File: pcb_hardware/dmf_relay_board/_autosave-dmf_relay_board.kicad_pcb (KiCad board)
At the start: 2 copper layers, 100 x 100 mm, 9 parts, among them J1 HVPS, J2 Relays to Electrodes 1, J3 Relays to Electrodes 2, J4 Electrodes from Relay 1, J5 Electrodes from Relay 2, U1 HV507

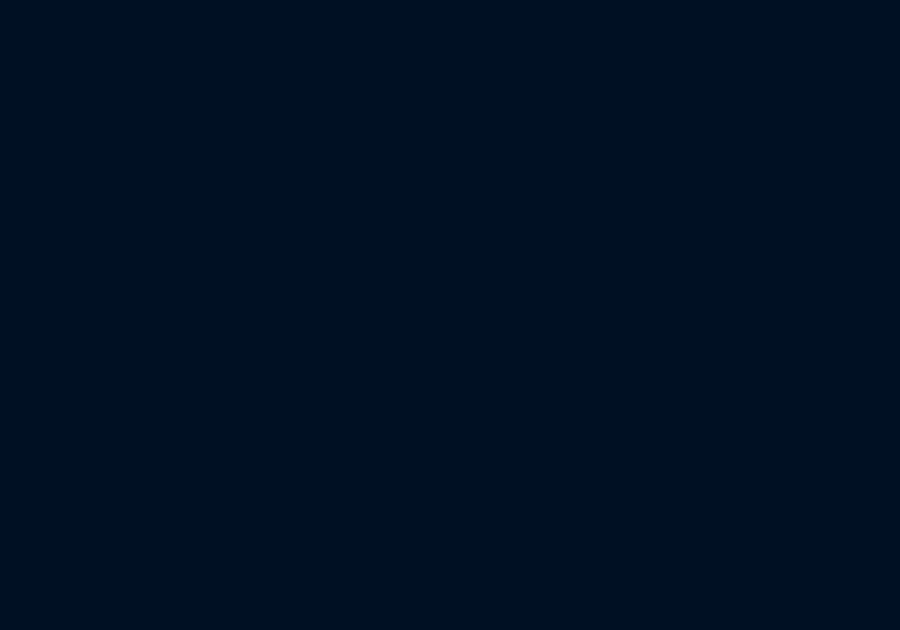
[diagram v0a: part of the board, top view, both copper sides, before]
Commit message: small footprint added
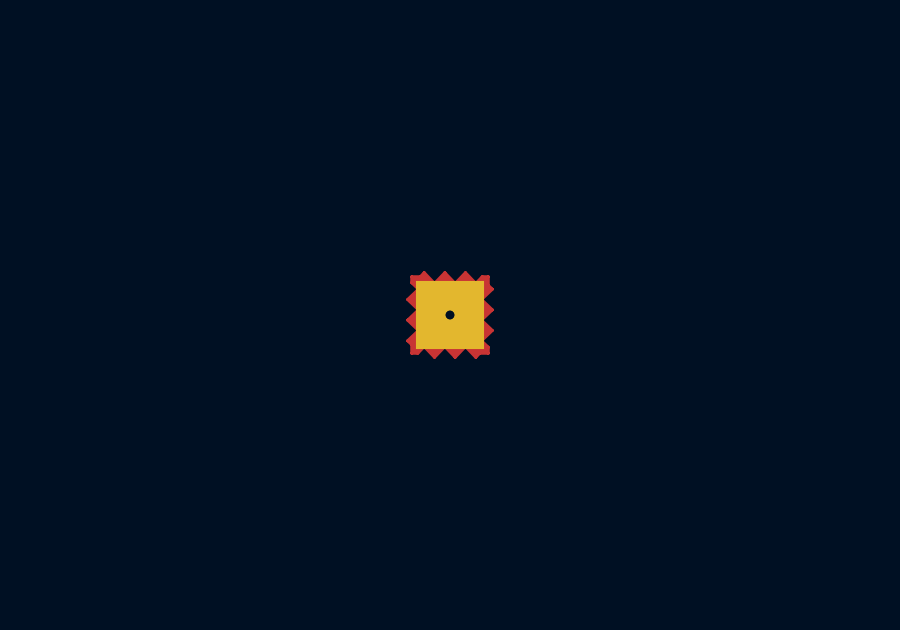
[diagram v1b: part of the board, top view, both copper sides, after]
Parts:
- added E1: ELEC_SML, dmf_relay_board:ELECTRODE_2_75_4MIL_4_5, F.Cu at (152.1, 65.3)
